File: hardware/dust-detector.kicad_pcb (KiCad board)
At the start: 2 copper layers, 50 x 50 mm, 34 parts, among them K1 CONN_3, K2 CONN_3, P1 CON-SENSOR, P2 CONN_6, Q1 2N7002P, U1 M24C64, U2 FAN4860, U3 TLV271, U4 DRILL, U5 DRILL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

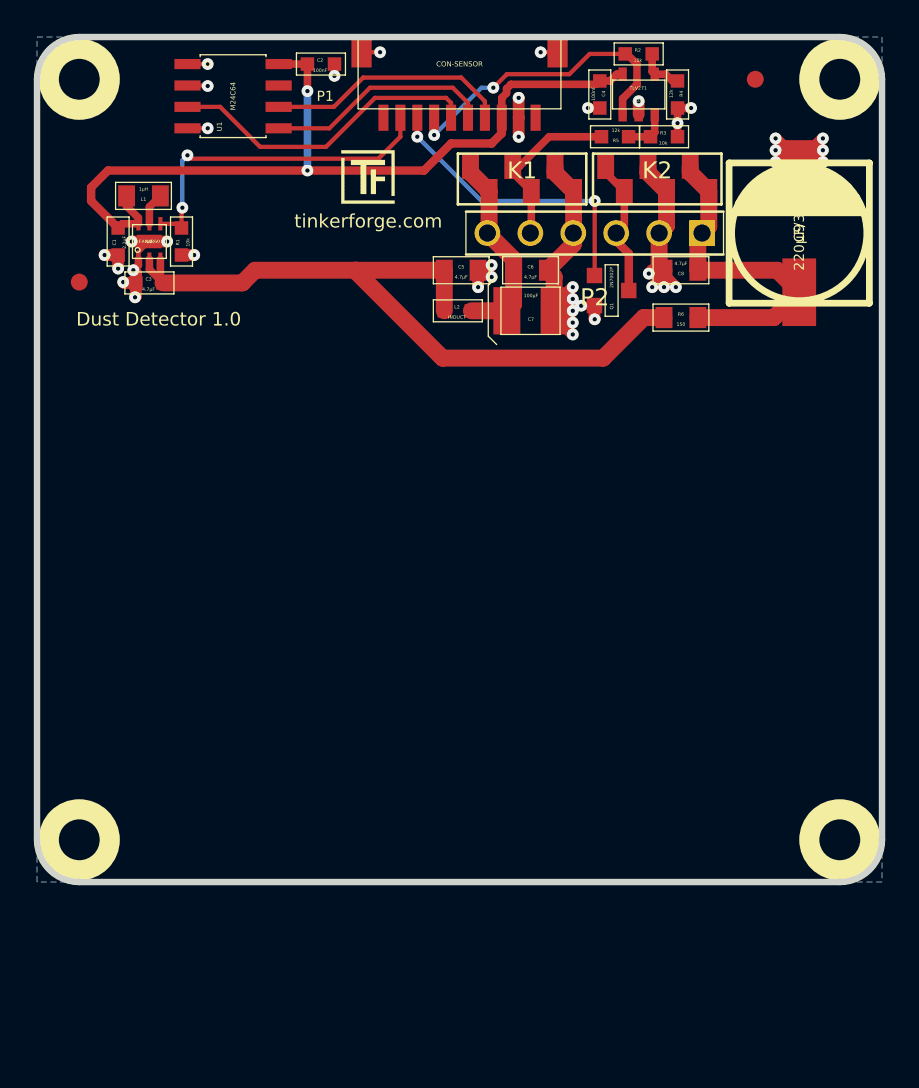
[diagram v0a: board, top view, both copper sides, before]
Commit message: change capacitor footprints change pcb size
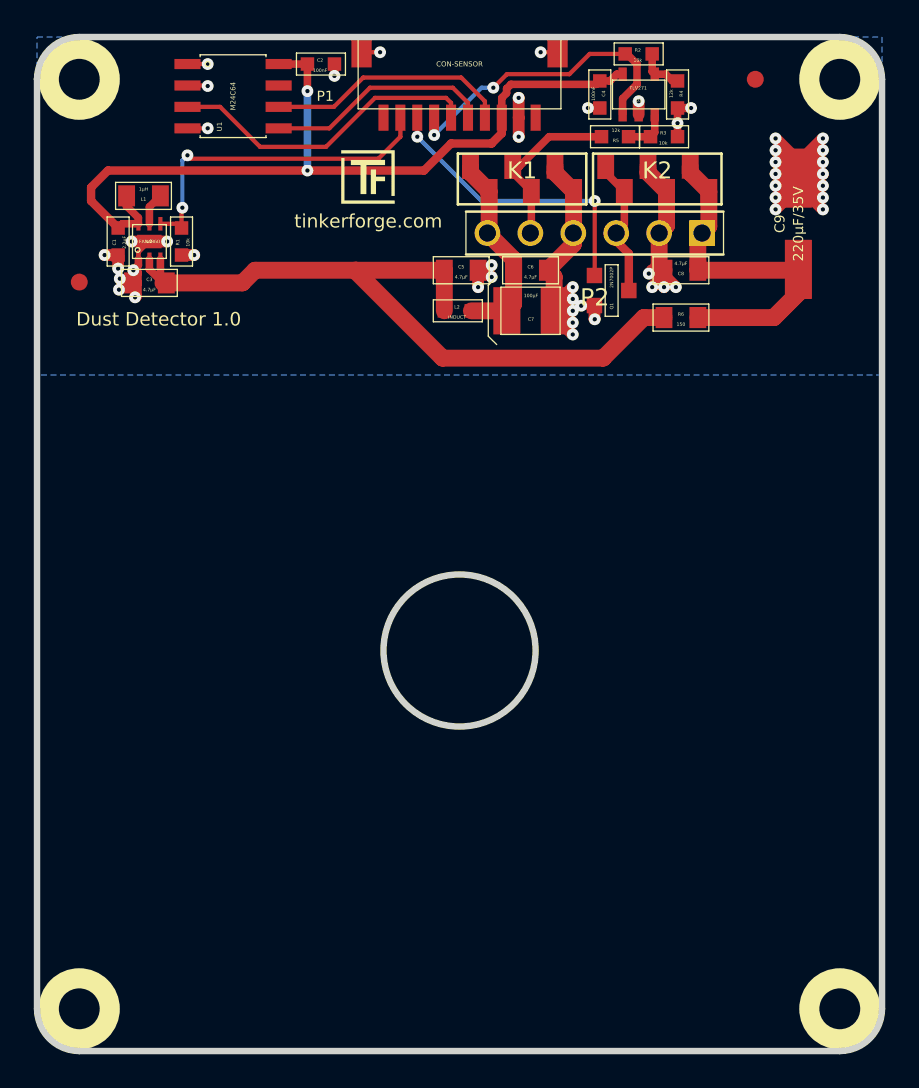
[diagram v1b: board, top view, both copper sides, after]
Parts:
- C3: footprint kicad-libraries:0603 -> kicad-libraries:0805
- C9: footprint kicad-libraries:ELKO_83 -> kicad-libraries:ELKO_63
- moved U4 10.0 mm to (121.4, 120.6)
- moved U7 10.0 mm to (166.4, 120.6)
- moved VAL 4.92 mm to (135.9, 91.6)
- moved VAL 4.92 mm to (151.9, 91.6)
- moved C9 0.55 mm to (163.9, 74.2)
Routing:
- net Net-(C8-Pad2): track 20.0 -> 22.9 mm
- net GND: track 81.4 -> 82.7 mm, vias 48 -> 49
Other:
- board size 50 x 50 mm -> 50 x 60 mm

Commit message: mark capacitor as dnp
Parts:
- C8: value 4.7µF -> DNP

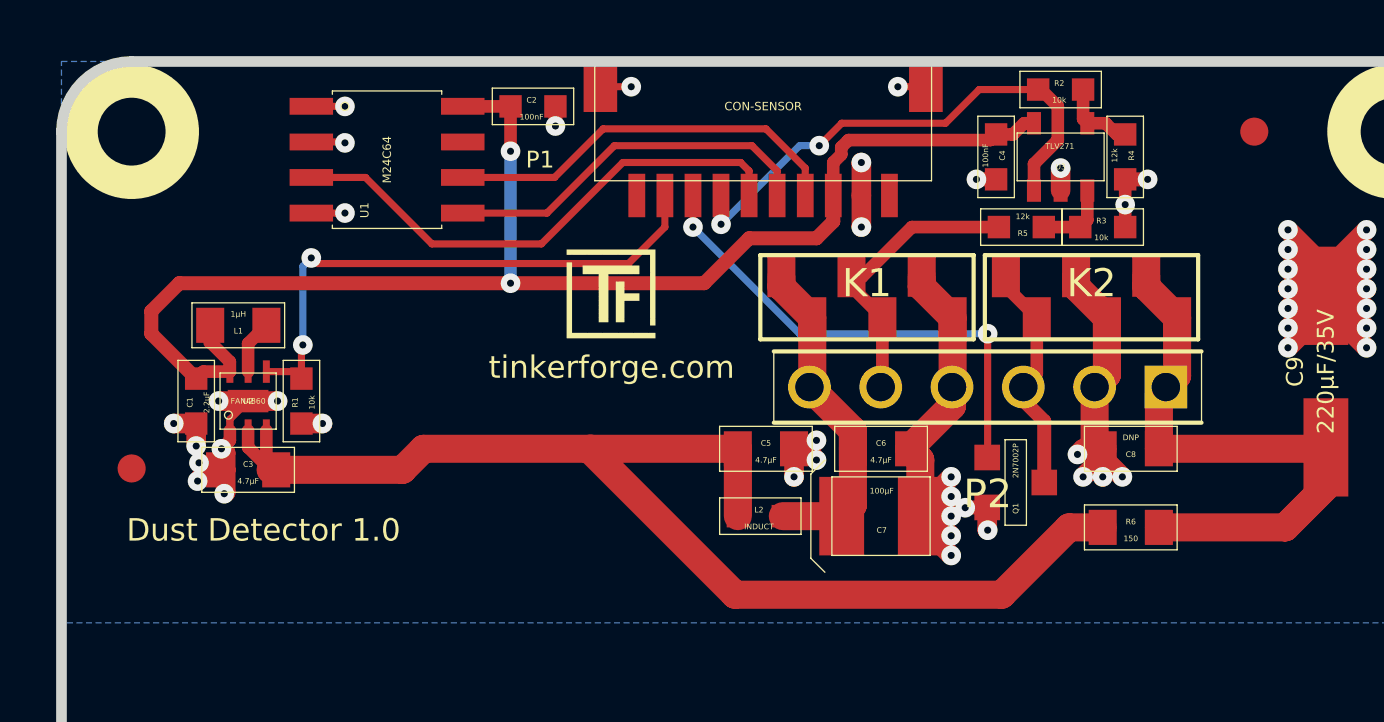
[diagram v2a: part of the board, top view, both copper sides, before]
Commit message: dust detector version 1.1 with tht connector
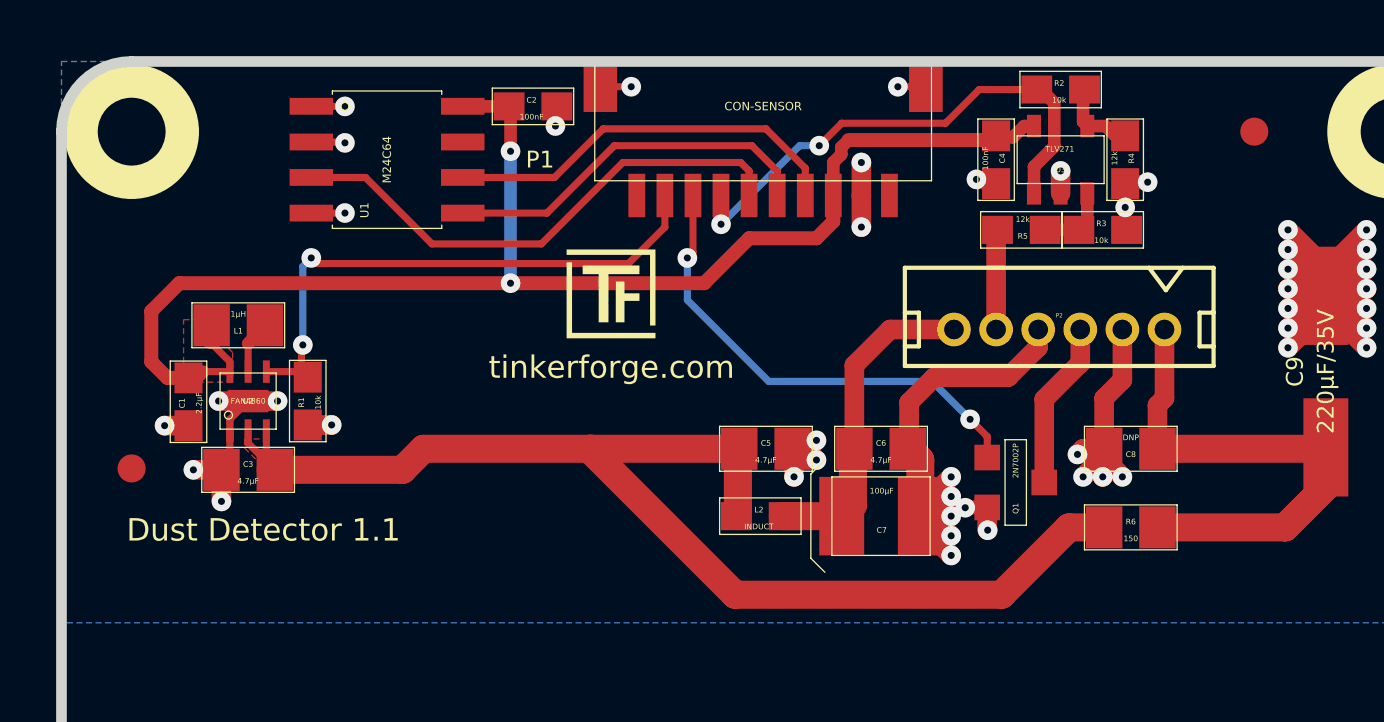
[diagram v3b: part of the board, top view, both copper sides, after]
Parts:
- removed K1, K2: CONN_3, kicad-libraries:9175-003
- C1, C2, C4, L2, R1, R2, R3, R4, R5: footprint kicad-libraries:0603 -> kicad-libraries:0603E
- C3, C5, C6, C8, L1, R6: footprint kicad-libraries:0805 -> kicad-libraries:0805E
- P2: footprint kicad-libraries:pin_array_6x1 -> kicad-libraries:B6B-ZR
- moved P2 3.27 mm to (154.4, 72.7)
- moved C1 0.28 mm to (123.4, 75.2)
- moved R1 0.22 mm to (127.7, 75.2)
- moved C4 0.10 mm to (152.2, 66.6)
- moved R3 0.10 mm to (156.0, 69.1)
- moved R4 0.10 mm to (156.8, 66.6)
- moved R5 0.10 mm to (153.1, 69.1)
- moved U3 0.10 mm to (154.5, 66.6)
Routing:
- net Net-(P2-Pad5): track 10.4 -> 3.57 mm
- net Net-(C8-Pad2): track 22.9 -> 20.4 mm
- net GND: track 82.7 -> 80.4 mm, vias 49 -> 46
- net Net-(P2-Pad3): track 8.29 -> 5.98 mm
- net 3V3: track 49.9 -> 50.9 mm
- added copper zone on F.Cu, net +5V
- added copper zone on F.Cu, net 3V3
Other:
- board text added: "Dust Detector 1.1"
- board text removed: "Dust Detector 1.0"

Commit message: Add 3d information (final)
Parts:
- added REF**: GP2Y1010AU0F, kicad-libraries:GP2Y1010AU0F, F.Cu at (144.0, 99.9)
- C1, C2, C4, L2: footprint kicad-libraries:0603E -> kicad-libraries:C0603E
- C3, C5, C6, C8, L1: footprint kicad-libraries:0805E -> kicad-libraries:C0805E
- R1, R2, R3, R4, R5: footprint kicad-libraries:0603E -> kicad-libraries:R0603E
- R6: footprint kicad-libraries:0805E -> kicad-libraries:R0805E
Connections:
- P1 pad 1: (no net) -> Net-(P1-Pad1)
- P1 pad 10: (no net) -> Net-(P1-Pad10)
- U1 pad 7: (no net) -> Net-(U1-Pad7)
